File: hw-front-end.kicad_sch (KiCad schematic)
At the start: 18 parts, among them J1 DB25_Pins, U1 USBLC6-4SC6, U2 USBLC6-4SC6, U3 USBLC6-4SC6

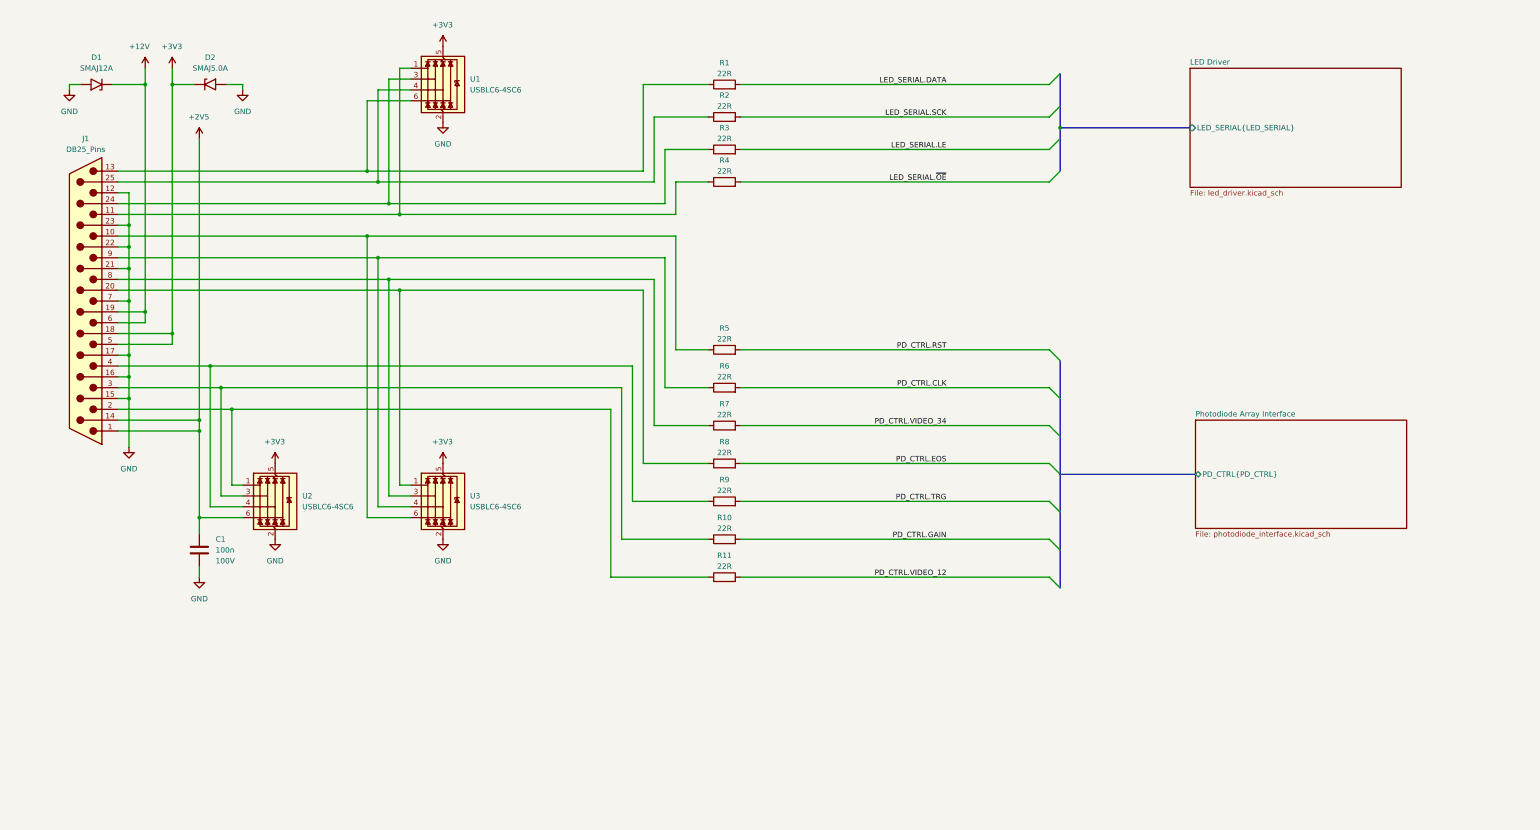
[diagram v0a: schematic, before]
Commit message: nodified according to review
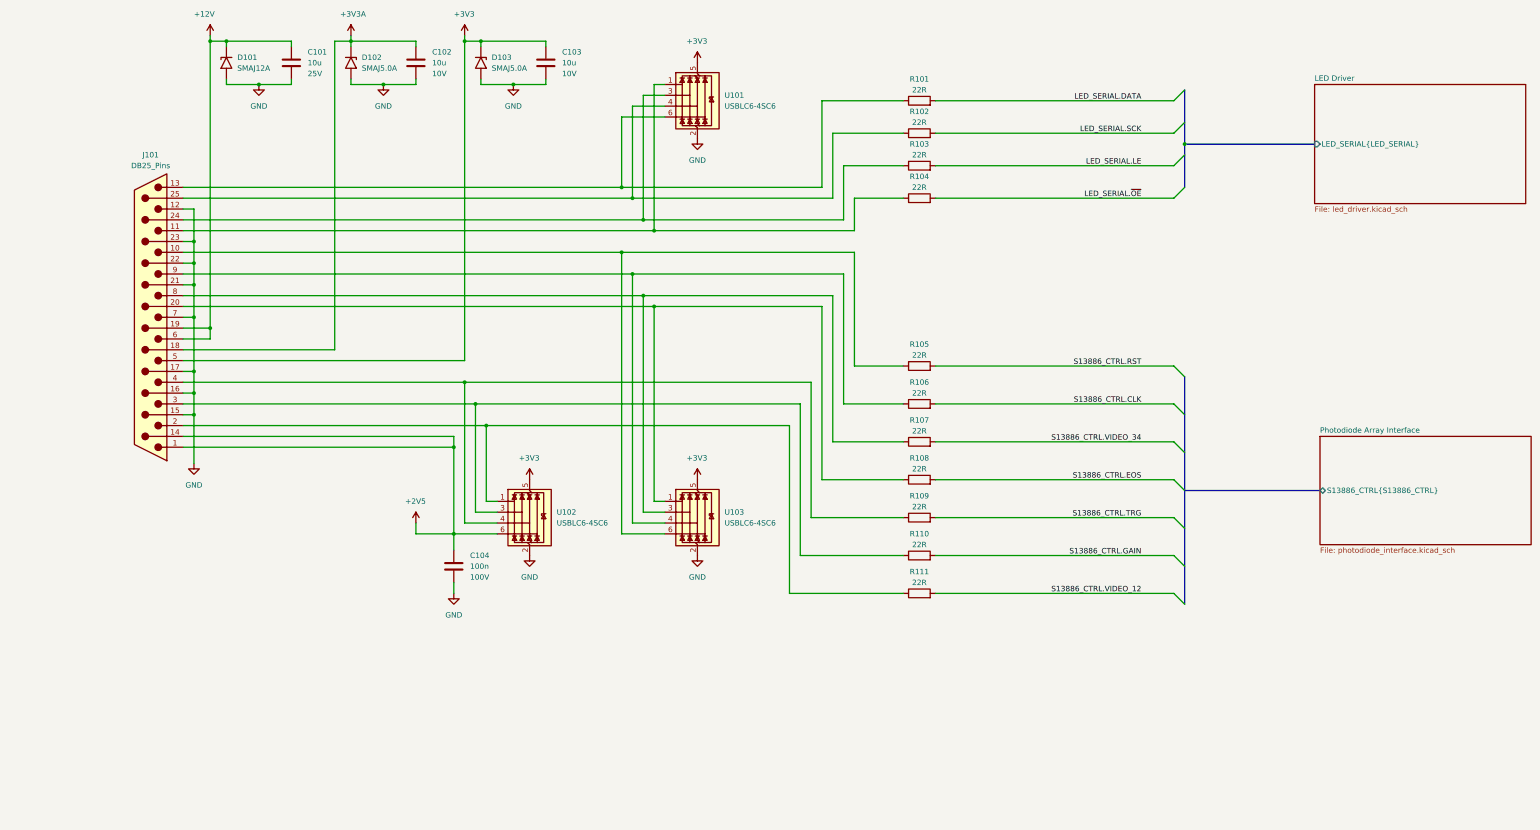
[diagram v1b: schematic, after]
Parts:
- added C101, C102, C103: 10u, symbol Capacitor_Protonica:C_voltage
- added D102: SMAJ5.0A, Diode_SMD:D_SMA, symbol Diode:SMAJ5.0A
- renumbered C1 to C104, D1 to D101, D2 to D103, J1 to J101, R1 to R101, R2 to R102, R3 to R103, R4 to R104, R5 to R105, R6 to R106, R7 to R107, R8 to R108, R9 to R109, R10 to R110, R11 to R111, U1 to U101, U2 to U102, U3 to U103
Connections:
- net +12V: now also C101.1
- net +3V3: now also C103.1; no longer J101.18 (P18)
- net GND: now also C101.2, C102.2, C103.2, D102.2 (A2)
- net PD_CTRL.CLK renamed S13886_CTRL.CLK
- net PD_CTRL.EOS renamed S13886_CTRL.EOS
- net PD_CTRL.GAIN renamed S13886_CTRL.GAIN
- net PD_CTRL.RST renamed S13886_CTRL.RST
- net PD_CTRL.TRG renamed S13886_CTRL.TRG
- net PD_CTRL.VIDEO_12 renamed S13886_CTRL.VIDEO_12
- net PD_CTRL.VIDEO_34 renamed S13886_CTRL.VIDEO_34
- new net +3V3A: C102.1, D102.1 (A1), J101.18 (P18)
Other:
- sheet Photodiode Array Interface ports: added S13886_CTRL{S13886_CTRL}; removed PD_CTRL{PD_CTRL}
- title: Adapter Card -> Front End Electronics
- moved on the sheet: C104, D101, D103, J101, R101, R102, R103, R104, R105, R106, R107, R108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

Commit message: footprints associated to symbols
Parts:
- removed J101: DB25_Pins, symbol Connector:DB25_Pins
- added C105: DNP, Capacitor_SMD:C_1206_3216Metric_Pad1.33x1.80mm_HandSolder, symbol Capacitor_Protonica:C_voltage
- added H101, H102, H103, H104: MountingHole_Pad, MountingHole:MountingHole_3.2mm_M3_Pad, symbol Mechanical:MountingHole_Pad
- added J102: DSUB-25, Connector_DSUB_THT_Wurth:J_Wurth_WR-DSUB_618025231221, symbol Connector_Protonica:DB25_Pins_MountingHoles_Wuerth
- added R112: DNP, Resistor_SMD:R_0805_2012Metric_Pad1.20x1.40mm_HandSolder, symbol Device:R
- C101: footprint (none) -> Capacitor_SMD:C_1206_3216Metric_Pad1.33x1.80mm_HandSolder; MPN (none) -> GRM31CR71E106KA12L; Manufacturer (none) -> Murata Electronics
- C102, C103: footprint (none) -> Capacitor_SMD:C_1206_3216Metric_Pad1.33x1.80mm_HandSolder; MPN (none) -> GRM31CR71E106KA12L; Manufacturer (none) -> Murata Electronics; Voltage 10V -> 25V
- C104: footprint (none) -> Capacitor_SMD:C_0805_2012Metric_Pad1.18x1.45mm_HandSolder; MPN (none) -> GCM21BR72A104KA37L; Manufacturer (none) -> Murata Electronics
- D101: MPN (none) -> SMAJ12A; Manufacturer (none) -> Littlefuse
- D102, D103: MPN (none) -> SMAJ5.0A; Manufacturer (none) -> Littlefuse
- R101, R102, R103, R104, R105, R106, R107, R108, R109, R110, R111: footprint (none) -> Resistor_SMD:R_0805_2012Metric_Pad1.20x1.40mm_HandSolder; MPN (none) -> CRCW080522R0FKEA; Manufacturer (none) -> Vishay Dale
- U101, U102, U103: MPN (none) -> USBLC6-4SC6; Manufacturer (none) -> STMicroelectronics
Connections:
- net +12V: now also J102.19 (P19), J102.6
- net +2V5: now also J102.1, J102.14 (P14)
- net +3V3: now also J102.5
- net +3V3A: now also J102.18 (P18)
- net GND: now also C105.2, J102.12, J102.15 (P15), J102.16 (P16), J102.17 (P17), J102.21 (P21), J102.22 (P22), J102.23 (P23), J102.7, R112.2
- net at R111.1, U102.1 (I/O1): now also J102.2
- net at R106.1, U103.4 (I/O3): now also J102.9
- net at R110.1, U102.3 (I/O2): now also J102.3
- net at R102.1, U101.4 (I/O3): now also J102.25 (P25)
- net at R105.1, U103.6 (I/O4): now also J102.10
- net at R109.1, U102.4 (I/O3): now also J102.4
- net at R104.1, U101.1 (I/O1): now also J102.11
- net at R101.1, U101.6 (I/O4): now also J102.13
- net at R108.1, U103.1 (I/O1): now also J102.20 (P20)
- net at R103.1, U101.3 (I/O2): now also J102.24 (P24)
- net at R107.1, U103.3 (I/O2): now also J102.8
- new net: C105.1, J102.S1 (SHIELD), J102.S2 (SHIELD), R112.1
- no-connect marks 0 -> 4

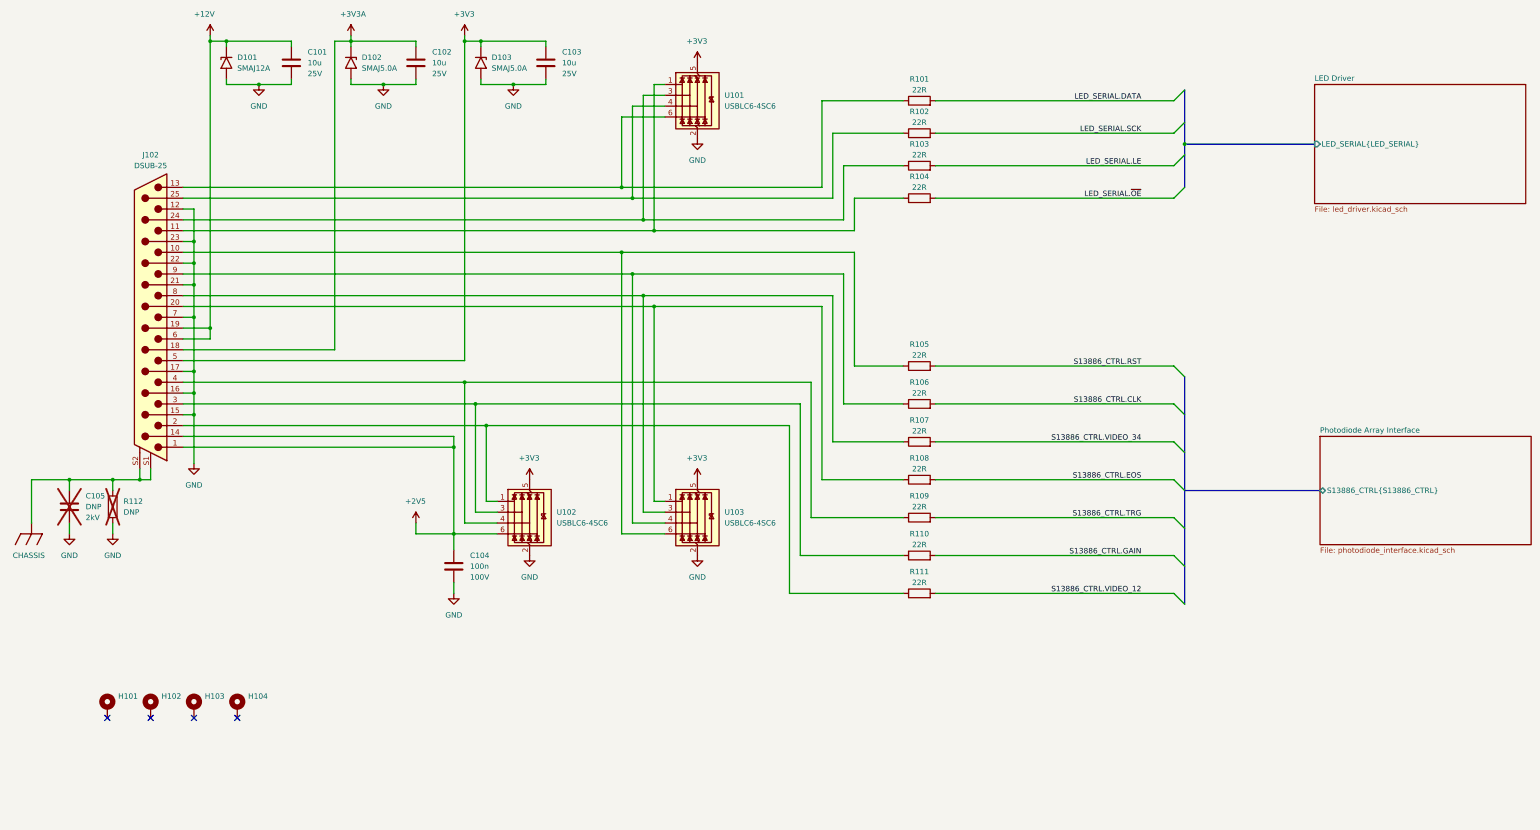
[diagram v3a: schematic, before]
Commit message: Most tracks routed
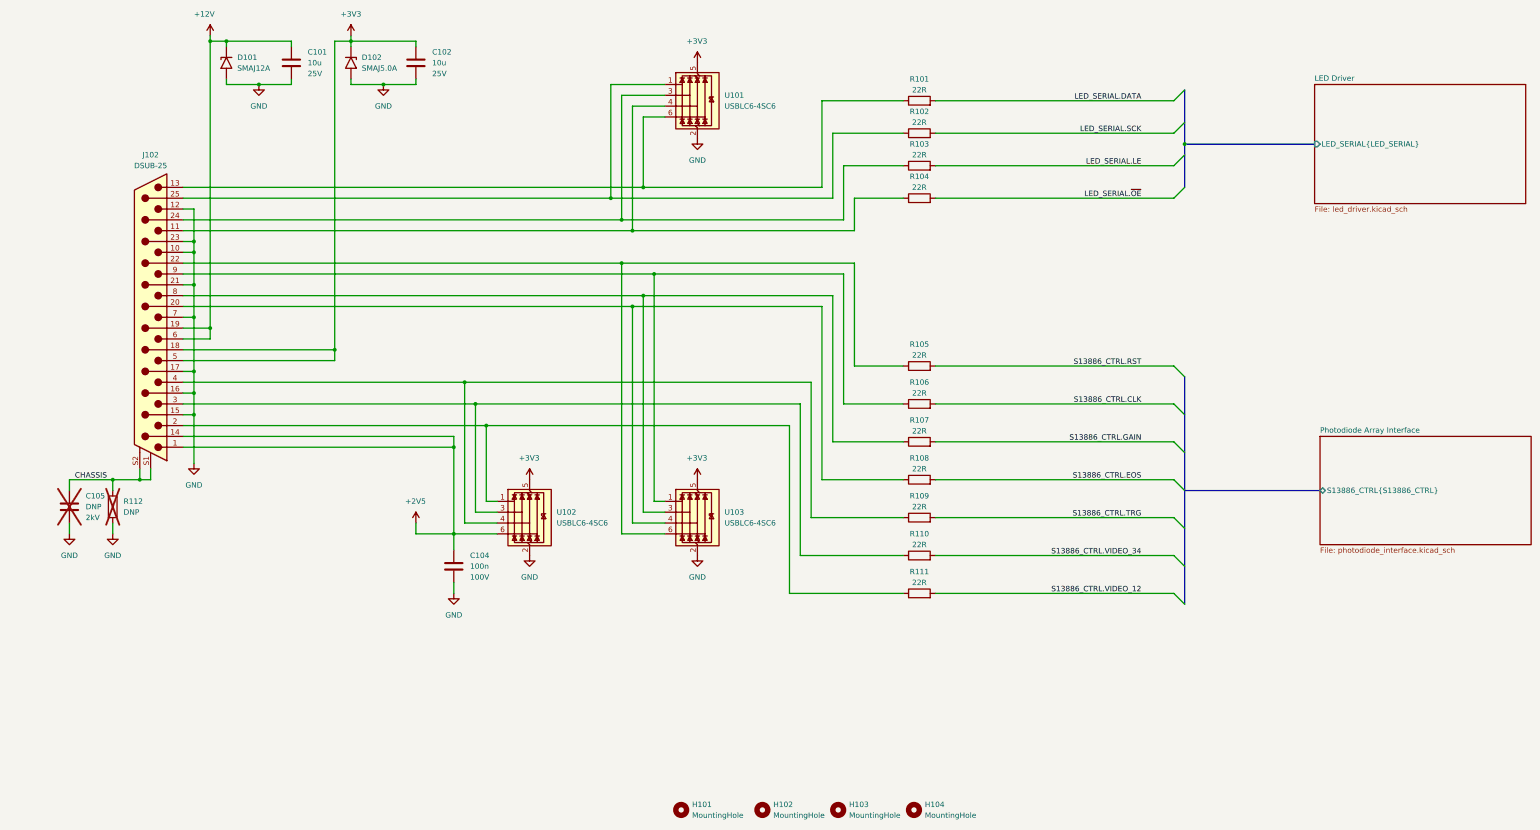
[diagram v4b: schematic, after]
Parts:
- removed C103: 10u, Capacitor_SMD:C_1206_3216Metric_Pad1.33x1.80mm_HandSolder, symbol Capacitor_Protonica:C_voltage
- removed D103: SMAJ5.0A, Diode_SMD:D_SMA, symbol Diode:SMAJ5.0A
- removed H101, H102, H103, H104: MountingHole_Pad, MountingHole:MountingHole_3.2mm_M3_Pad, symbol Mechanical:MountingHole_Pad
- added H101, H102, H103, H104: MountingHole, MountingHole:MountingHole_3.2mm_M3_DIN965, symbol Mechanical:MountingHole
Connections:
- net +3V3A is gone; now on net +3V3: C102.1, D102.1 (A1), J102.18 (P18)
- net GND: now also J102.10; no longer J102.22 (P22)
- net S13886_CTRL.GAIN: now also R107.2; no longer R110.2
- net S13886_CTRL.VIDEO_34: now also R110.2; no longer R107.2
- net at J102.9, R106.1: now also U103.1 (I/O1); no longer U103.4 (I/O3)
- net at J102.25 (P25), R102.1: now also U101.1 (I/O1); no longer U101.4 (I/O3)
- net at R105.1, U103.6 (I/O4): now also J102.22 (P22); no longer J102.10
- net at J102.11, R104.1: now also U101.4 (I/O3); no longer U101.1 (I/O1)
- net at J102.20 (P20), R108.1: now also U103.4 (I/O3); no longer U103.1 (I/O1)
- net CHASSIS: now reaches C105.1, J102.S1 (SHIELD), J102.S2 (SHIELD), R112.1
- no-connect marks 4 -> 0

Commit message: DRC clean
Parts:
- R112: footprint Resistor_SMD:R_0805_2012Metric_Pad1.20x1.40mm_HandSolder -> Resistor_SMD:R_1206_3216Metric_Pad1.30x1.75mm_HandSolder
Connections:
- net +2V5: now also U102.1 (I/O1); no longer U102.6 (I/O4)
- net CHASSIS: no longer J102.S1 (SHIELD)
- net at J102.2, R111.1: now also U102.6 (I/O4); no longer U102.1 (I/O1)
- net at J102.3, R110.1: now also U102.4 (I/O3); no longer U102.3 (I/O2)
- net at J102.4, R109.1: now also U102.3 (I/O2); no longer U102.4 (I/O3)
- no-connect marks 0 -> 1
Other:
- moved on the sheet: C104

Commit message: minor changes
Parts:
- D101, D102: Manufacturer Littlefuse -> Littelfuse
- J102: Manufacturer Würth Elektronik -> Wurth Elektronik
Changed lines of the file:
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@@
 			)
 		)
-		(property "Manufacturer" "Würth Elektronik"
+		(property "Manufacturer" "Wurth Elektronik"
 			(at 55.88 133.35 0)
 			(hide yes)
@@
 			)
 		)
-		(property "Manufacturer" "Littlefuse"
+		(property "Manufacturer" "Littelfuse"
 			(at 73.66 73.66 90)
 			(hide yes)
@@
 			)
 		)
-		(property "Manufacturer" "Littlefuse"
+		(property "Manufacturer" "Littelfuse"
 			(at 102.87 73.66 90)
 			(hide yes)
